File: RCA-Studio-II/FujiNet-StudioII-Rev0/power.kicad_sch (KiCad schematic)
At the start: 21 parts, among them J3 USB-C, Q1 AO3401A, U6 AP2112K-3.3

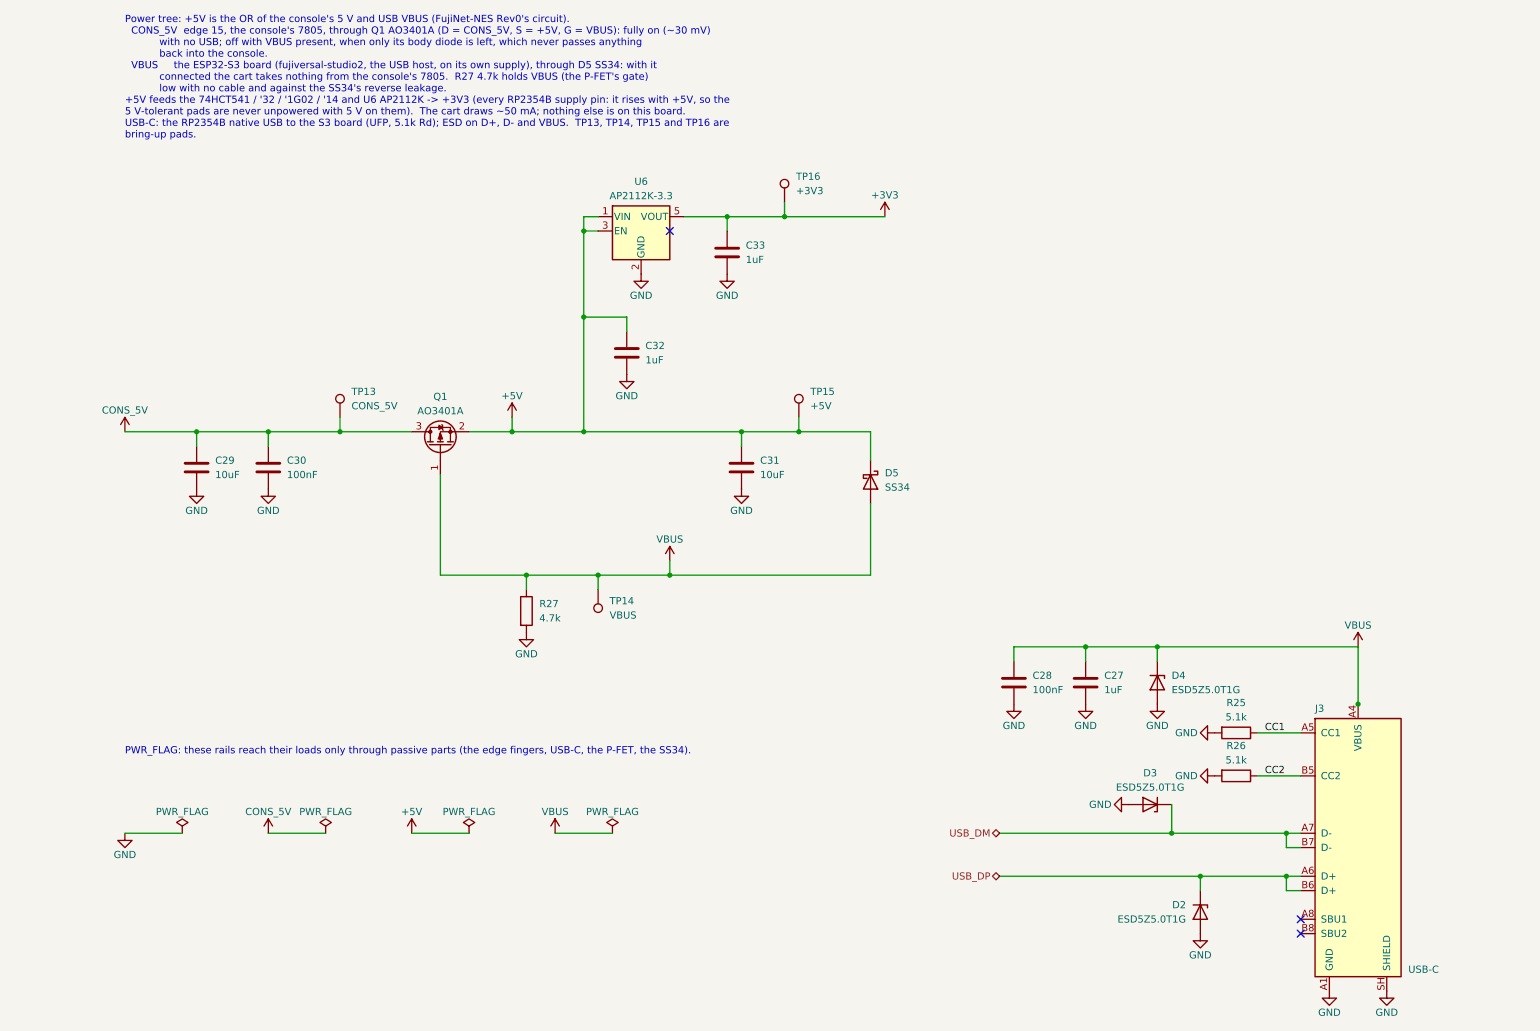
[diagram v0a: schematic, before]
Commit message: Studio II Rev0: ESP32-S3 on the cart, 4-layer board, JLCPCB package
The schematic is redone with the FujiNet's ESP32-S3 on the cartridge (it was
on a separate board), and the board is laid out, routed and audited for
JLCPCB assembly.

Schematic (5 sheets: cart-bus, rp-core, fujinet, usb, power):
- ESP32-S3-WROOM-1-N16R8 as the FujiNet and the RP2354B's USB host, with
  microSD, WS2812, EN RC and buttons (ported from FujiNet-ChannelF Rev0)
- USB-C -> USBLC6-2SC6 -> CP2102N with the UMH3N auto-program pair
- a TPS2116 power mux (USB first, the console's 5 V second) replaces the
  P-FET / SS34 OR, so the 74HCT glue stays at >= 4.72 V on either source
- AP63203 buck for the S3 side; RESET reaches both MCUs; the S3 drives the
  RP's RUN / BOOTSEL through 1k
- ERC 0, netlist parity 97 / 97, check_nets 364 / 0 failed / 1 warning
  (fujiversal-studio2.h lacks PIN_RP2040_RUN / _BOOTSEL), margins positive

Board: FliP's multicart outline from the insertion edge, 28 mm taller
(90.9 x 111.5 mm, printed shell), 22 hard-gold fingers on B.Cu, 4 layers,
every part on F.Cu; the S3 flush at the top edge with its antenna keep-out.
- KiCad DRC with schematic parity, all severities: 0 / 0 / 0, on the
  saved zone fills; layout_checks 65 / 65; check_fab 10 / 10
- LAYOUT=1 regenerates and re-routes it from scratch with every gate green

Fixes found by the audit, each now in the generator and gated:
- the gerbers plotted stale zone fills: 427 GND vias sat inside the In2
  power pours. tools/fill_zones.py refills after the last via, DRC runs
  on the saved fills, export uses --check-zones, and check_gerbers.py
  check 9 tests every plated hole against the plotted inner layers
- a 20 mm D+ loop at the flow-through USBLC6: twin pins now joined under
  the body, its 100 nF moved to the VBUS pin as ST draws it
- the USB-C 1.35 mm inside the edge: moved to HRO's layout (face 0.46 mm
  past the edge), USB-C and microSD 3D models fixed (FujiNet-NES 63ccf57)
- the antenna keep-out added as board ru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
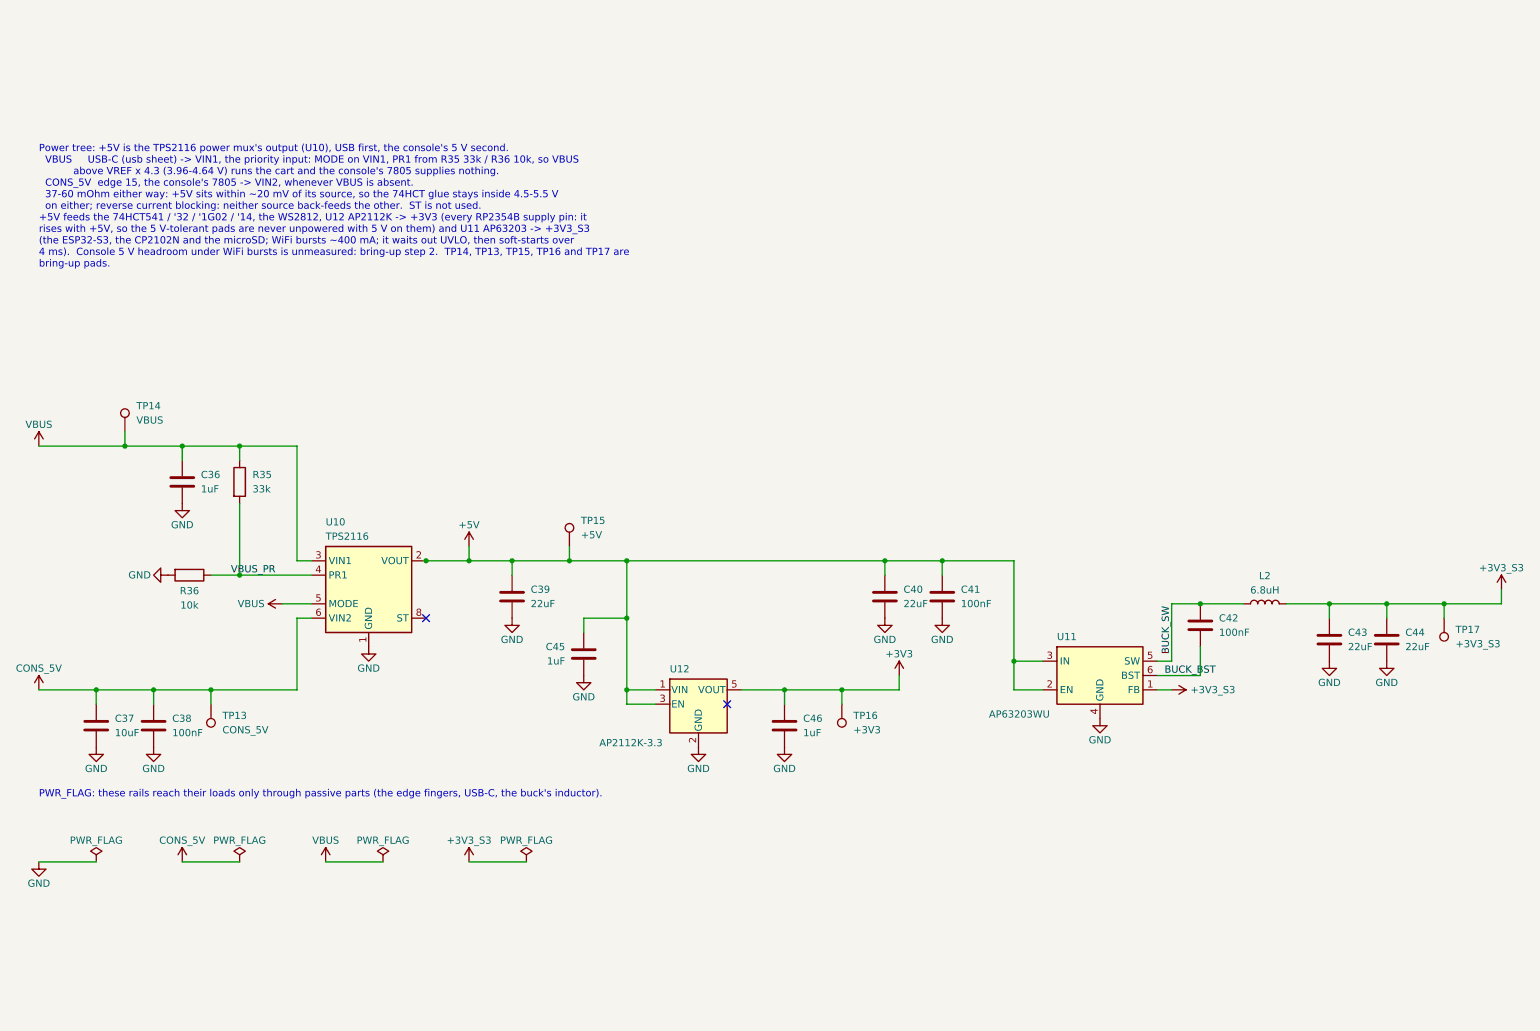
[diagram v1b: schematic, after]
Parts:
- removed C27, C32, C33: 1uF, FujiNet-StudioII:C_0603_1608Metric, symbol Device:C
- removed C28, C30: 100nF, FujiNet-StudioII:C_0603_1608Metric, symbol Device:C
- removed C29, C31: 10uF, FujiNet-StudioII:C_0603_1608Metric, symbol Device:C
- removed D2, D3, D4: ESD5Z5.0T1G, FujiNet-StudioII:D_SOD-523, symbol Diode:ESD5Zxx
- removed D5: SS34, FujiNet-StudioII:D_SMA, symbol Diode:SS34
- removed J3: USB-C, FujiNet-StudioII:USB_C_Receptacle_HRO_TYPE-C-31-M-12, symbol FujiNet-StudioII:USB_C_USB2.0_16P_Fn
- removed Q1: AO3401A, FujiNet-StudioII:SOT-23, symbol Transistor_FET:AO3401A
- removed R25, R26: 5.1k, FujiNet-StudioII:R_0603_1608Metric, symbol Device:R
- removed R27: 4.7k, FujiNet-StudioII:R_0603_1608Metric, symbol Device:R
- removed U6: AP2112K-3.3, FujiNet-StudioII:SOT-23-5, symbol Regulator_Linear:AP2112K-3.3
- added C36, C45, C46: 1uF, FujiNet-StudioII:C_0603_1608Metric, symbol Device:C
- added C37: 10uF, FujiNet-StudioII:C_0603_1608Metric, symbol Device:C
- added C38, C41, C42: 100nF, FujiNet-StudioII:C_0603_1608Metric, symbol Device:C
- added C39, C40, C43, C44: 22uF, FujiNet-StudioII:C_0805_2012Metric, symbol Device:C
- added L2: 6.8uH, FujiNet-StudioII:L_Sunlord_SWPA4030S, symbol Device:L
- added R35: 33k, FujiNet-StudioII:R_0603_1608Metric, symbol Device:R
- added R36: 10k, FujiNet-StudioII:R_0603_1608Metric, symbol Device:R
- added TP17: +3V3_S3, FujiNet-StudioII:TestPoint_Pad_D1.5mm, symbol Connector:TestPoint
- added U10: TPS2116, FujiNet-StudioII:SOT-583-8, symbol Power_Management:TPS2116DRL
- added U11: AP63203WU, FujiNet-StudioII:TSOT-23-6, symbol Regulator_Switching:AP63203WU
- added U12: AP2112K-3.3, FujiNet-StudioII:SOT-23-5, symbol Regulator_Linear:AP2112K-3.3
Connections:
- net +3V3: now also C46.1, U12.5 (VOUT)
- net +5V: now also C39.1, C40.1, C41.1, C45.1, U10.2 (VOUT), U10.7 (VOUT), U11.2 (EN), U11.3 (IN), U12.1 (VIN), U12.3 (EN)
- net CONS_5V: now also C37.1, C38.1, U10.6 (VIN2)
- net GND: now also C36.2, C37.2, C38.2, C39.2, C40.2, C41.2, C43.2, C44.2, C45.2, C46.2, R36.2, U10.1 (GND), U11.4 (GND), U12.2 (GND)
- net VBUS: now also C36.1, R35.1, U10.3 (VIN1), U10.5 (MODE)
- new net +3V3_S3: C43.1, C44.1, L2.2, TP17.1, U11.1 (FB)
- new net BUCK_BST: C42.2, U11.6 (BST)
- new net BUCK_SW: C42.1, L2.1, U11.5 (SW)
- new net VBUS_PR: R35.2, R36.1, U10.4 (PR1)
- no-connect marks 3 -> 2
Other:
- note added: "PWR_FLAG: these rails reach their loads only through passive parts (the edge fingers, USB-C, the buck's inductor)."
- note added: "Power tree: +5V is the TPS2116 power mux's output (U10), USB first, the console's 5 V second. VBUS USB-C (usb sheet) -> VIN1, the priority input: MODE on VIN1, PR1 from R35 33k / R36 10k, so VBUS above VREF x 4.3 (3.96-4.64 V) runs the cart and the console's 7805 supplies nothing. CONS_5V edge 15, the console's 7805 -> VIN2, whenever VBUS is absent. 37-60 mOhm either way: +5V sits within ~20 mV o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"
- note removed: "PWR_FLAG: these rails reach their loads only through passive parts (the edge fingers, USB-C, the P-FET, the SS34)."
- note removed: "Power tree: +5V is the OR of the console's 5 V and USB VBUS (FujiNet-NES Rev0's circuit). CONS_5V edge 15, the console's 7805, through Q1 AO3401A (D = CONS_5V, S = +5V, G = VBUS): fully on (~30 mV) with no USB; off with VBUS present, when only its body diode is left, which never passes anything back into the console. VBUS the ESP32-S3 board (fujiversal-studio2, the USB host, on its own supply), t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"
- title: FujiNet Studio II Rev0 - Power, RP LDO, USB-C to the S3 -> FujiNet Studio II Rev0 - Power: mux, S3 buck, RP LDO
- moved on the sheet: TP13, TP14, TP15, TP16
